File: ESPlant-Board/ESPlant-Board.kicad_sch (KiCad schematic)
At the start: 30 parts, among them J1 Conn_02x04_Counter_Clockwise, U1 ESP32-S2-MINI-1-N4, U2 BH-AAA-B5AK001, U3 Reset, U4 Boot, U5 Temp/Humid-Sensor, U6 Light sensor, U7 AMS1117-3_3, U8 MK-12C02-G025

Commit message: Update pcb for v2.0
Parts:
- removed D1: GREEN, LED_SMD:LED_0805_2012Metric, symbol Device:LED
- removed D2: ~, Diode_SMD:D_SOD-123, symbol Device:D
- removed D3: RED, LED_SMD:LED_0805_2012Metric, symbol Device:LED
- added D1: GREEN, CustomFootprints:LED0805-GREEN-RD, symbol Custom_Parts:Green-0805-LED
- added D2: SOD-123-Switching-Diode, CustomFootprints:SOD-123F_L2.7-W1.6-LS3.8-RD, symbol Custom_Parts:SOD-123-Switching-Diode
- added D3: RED, CustomFootprints:LED0805-RD_RED, symbol Custom_Parts:Red-0805-LED
- added H1, H2: MountingHole, CustomFootprints:JLCPCB_ToolingHole, symbol Mechanical:MountingHole
- added R10, R2: 5k1, Resistor_SMD:R_0402_1005Metric, symbol Device:R
- C4: now not fitted; now left out of the parts list
- U8: MPN (none) -> C778186
- USB1: now left out of the parts list
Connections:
- net +3V3: now also R10.2, R2.2
- net AD_Capacitance: now also D2.1 (K)
- net GND: now also D1.2 (K), D3.1 (-)
- net LED_GREEN: now also D1.1 (A)
- net LED_RED: now also D3.2 (+)
- net SensorCapV: now also D2.2 (A)
- net TH_SCL: now also R2.1
- net TH_SDA: now also R10.1

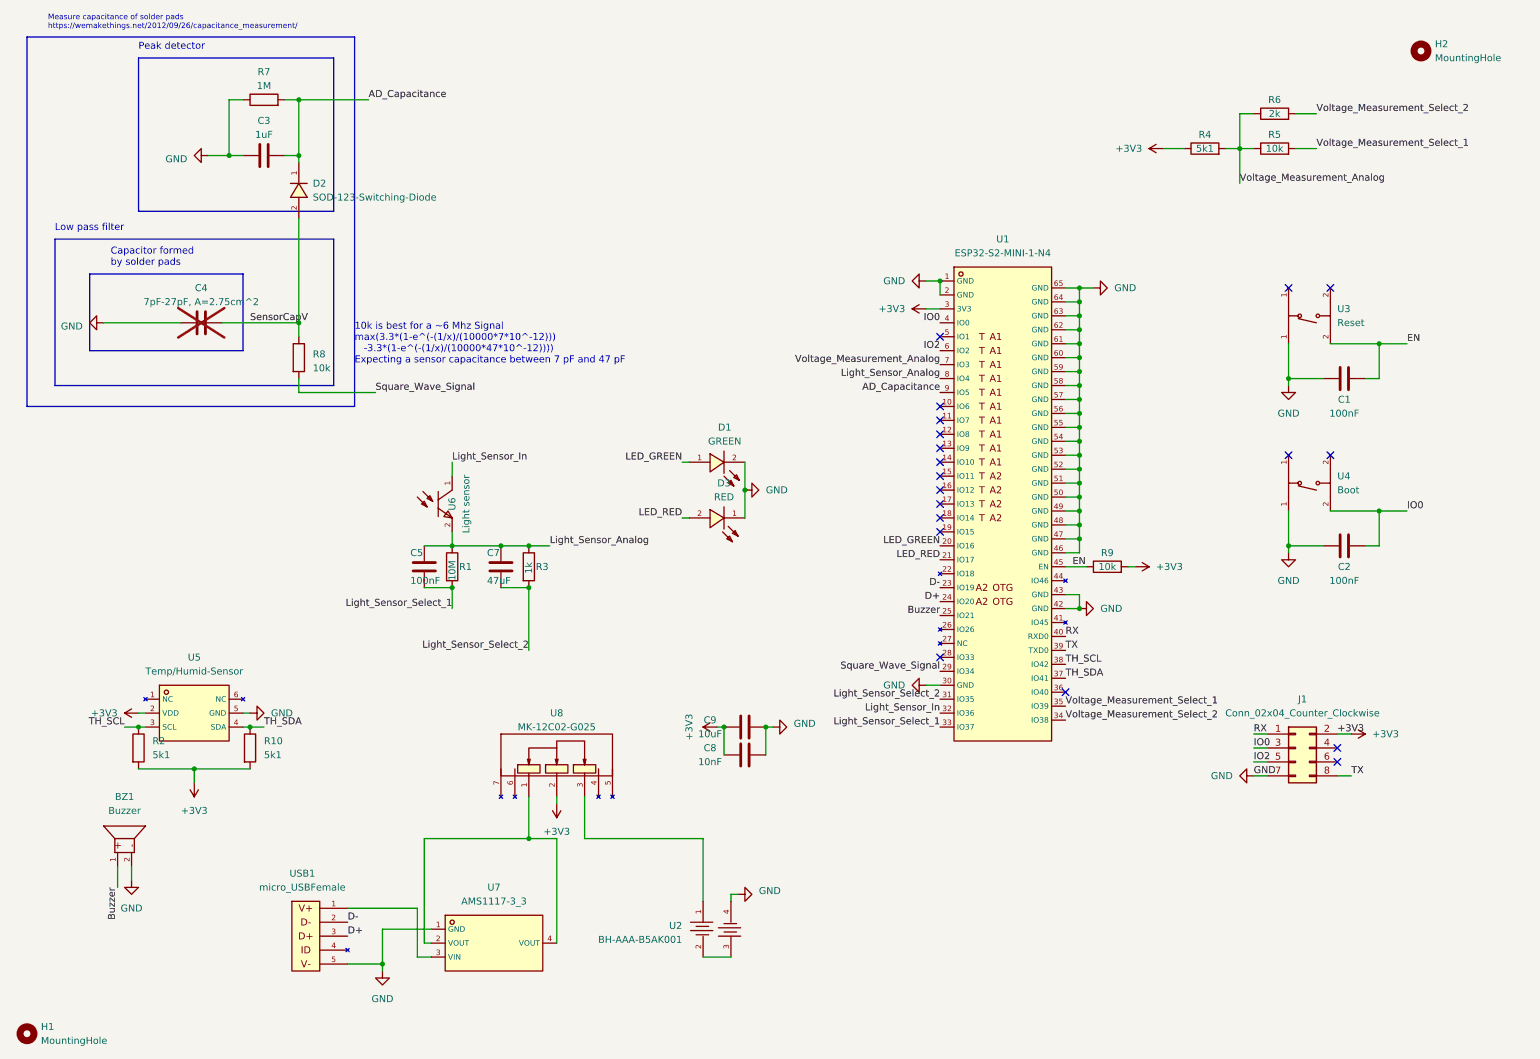
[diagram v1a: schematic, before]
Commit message: add fab layer
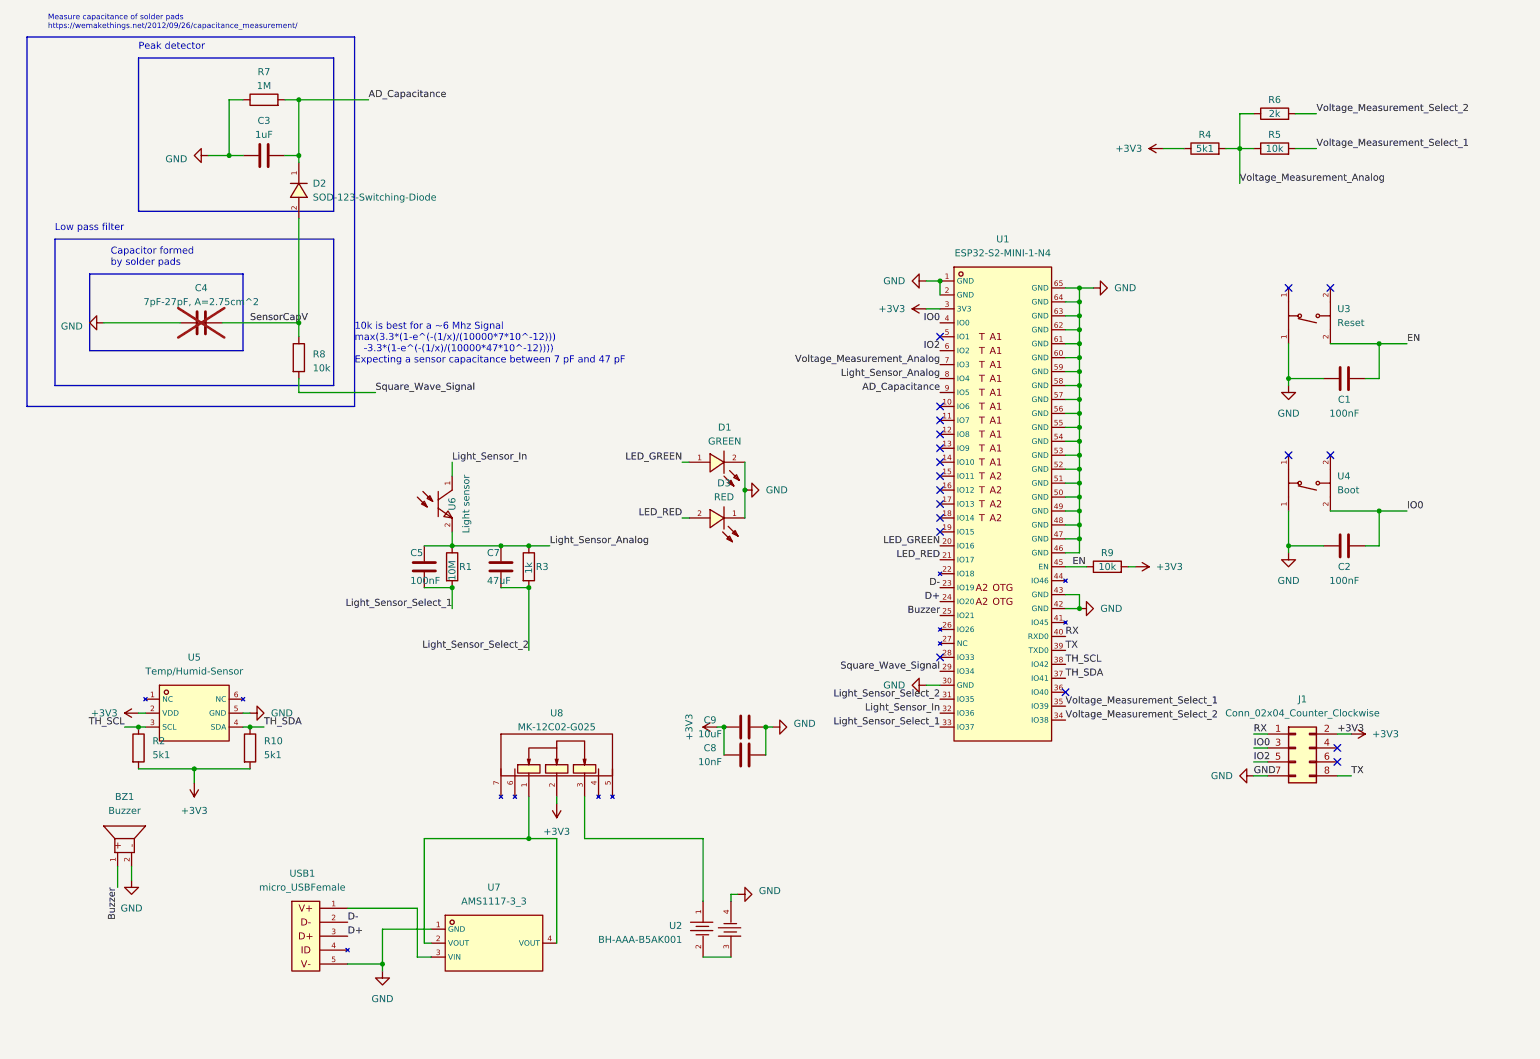
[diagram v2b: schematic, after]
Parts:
- removed H1, H2: MountingHole, CustomFootprints:JLCPCB_ToolingHole, symbol Mechanical:MountingHole
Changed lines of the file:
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@@
-    )
-  )
-  (symbol (lib_id "Mechanical:MountingHole") (at 15.24 194.31 0) (unit 1)
-    (in_bom yes) (on_board yes) (dnp no) (fields_autoplaced)
-    (property "Reference" "H1" (at 17.78 193.04 0)
-      (effects (font (size 1.27 1.27)) (justify left))
-    )
-    (property "Value" "MountingHole" (at 17.78 195.58 0)
-      (effects (font (size 1.27 1.27)) (justify left))
-    )
-    (property "Footprint" "CustomFootprints:JLCPCB_ToolingHole" (at 15.24 194.31 0)
-      (effects (font (size 1.27 1.27)) hide)
-    )
-    (property "Datasheet" "~" (at 15.24 194.31 0)
-      (effects (font (size 1.27 1.27)) hide)
-    )
-    (instances
-      (project "ESPlant-Board"
-        (path "/fa2a81f8-bf39-4c28-beef-a6fc807c4564"
-          (reference "H1") (unit 1)
-        )
-      )
     )
   )
@@
         )
       )
-    )
-  )
-  (symbol (lib_id "Mechanical:MountingHole") (at 269.24 15.24 0) (unit 1)
-    (in_bom yes) (on_board yes) (dnp no) (fields_autoplaced)
-    (property "Reference" "H2" (at 271.78 13.97 0)
-      (effects (font (size 1.27 1.27)) (justify left))
-    )
-    (property "Value" "MountingHole" (at 271.78 16.51 0)
-      (effects (font (size 1.27 1.27)) (justify left))
-    )
-    (property "Footprint" "CustomFootprints:JLCPCB_ToolingHole" (at 269.24 15.24 0)
-      (effects (font (size 1.27 1.27)) hide)
-    )
-    (property "Datasheet" "~" (at 269.24 15.24 0)
-      (effects (font (size 1.27 1.27)) hide)
-    )
-    (instances
-      (project "ESPlant-Board"
-        (path "/fa2a81f8-bf39-4c28-beef-a6fc807c4564"
-          (reference "H2") (unit 1)
-        )
-      )

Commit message: Add panel
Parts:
- J1: now left out of the parts list
- USB1: now in the parts list
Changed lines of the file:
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@@
   )
   (symbol (lib_id "Connector_Generic:Conn_02x04_Odd_Even") (at 246.38 142.24 0) (unit 1)
-    (in_bom yes) (on_board yes) (dnp no) (fields_autoplaced)
+    (in_bom no) (on_board yes) (dnp no) (fields_autoplaced)
     (property "Reference" "J1" (at 247.65 133.35 0)
       (effects (font (size 1.27 1.27)))
@@
   )
   (symbol (lib_id "Custom_Parts:micro_USBFemale") (at 64.77 176.53 0) (unit 1)
-    (in_bom no) (on_board yes) (dnp no) (fields_autoplaced)
+    (in_bom yes) (on_board yes) (dnp no) (fields_autoplaced)
     (property "Reference" "USB1" (at 65.405 165.1 0)
       (effects (font (size 1.27 1.27)))

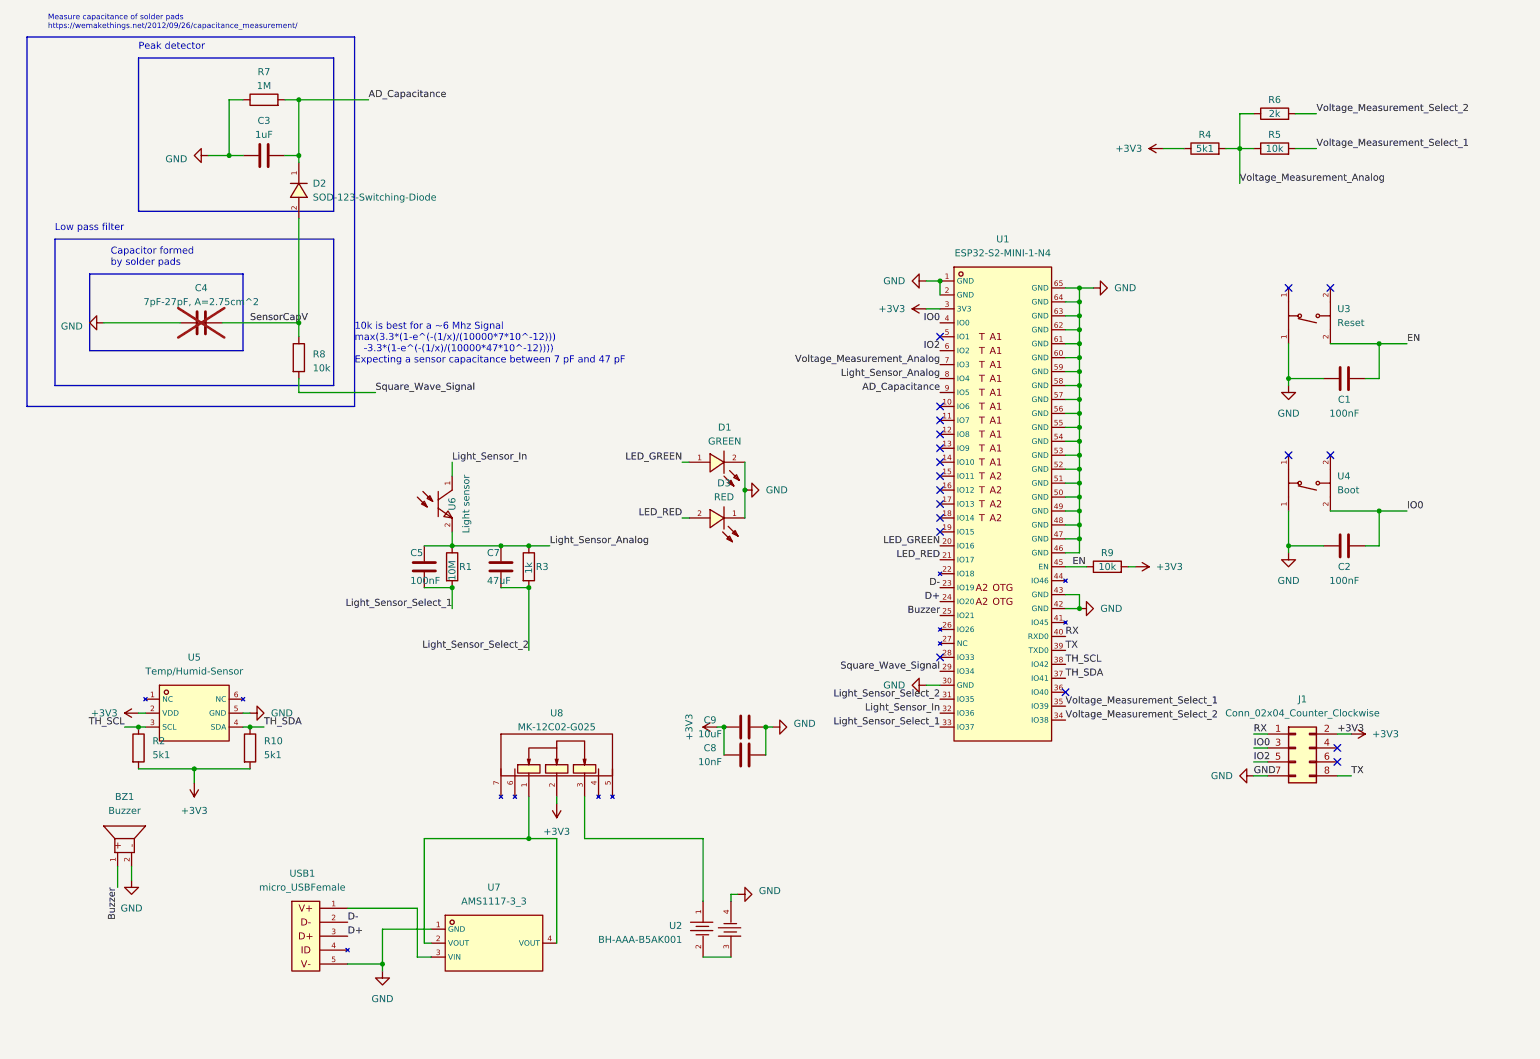
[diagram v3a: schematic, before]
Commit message: board: remove redundant parts
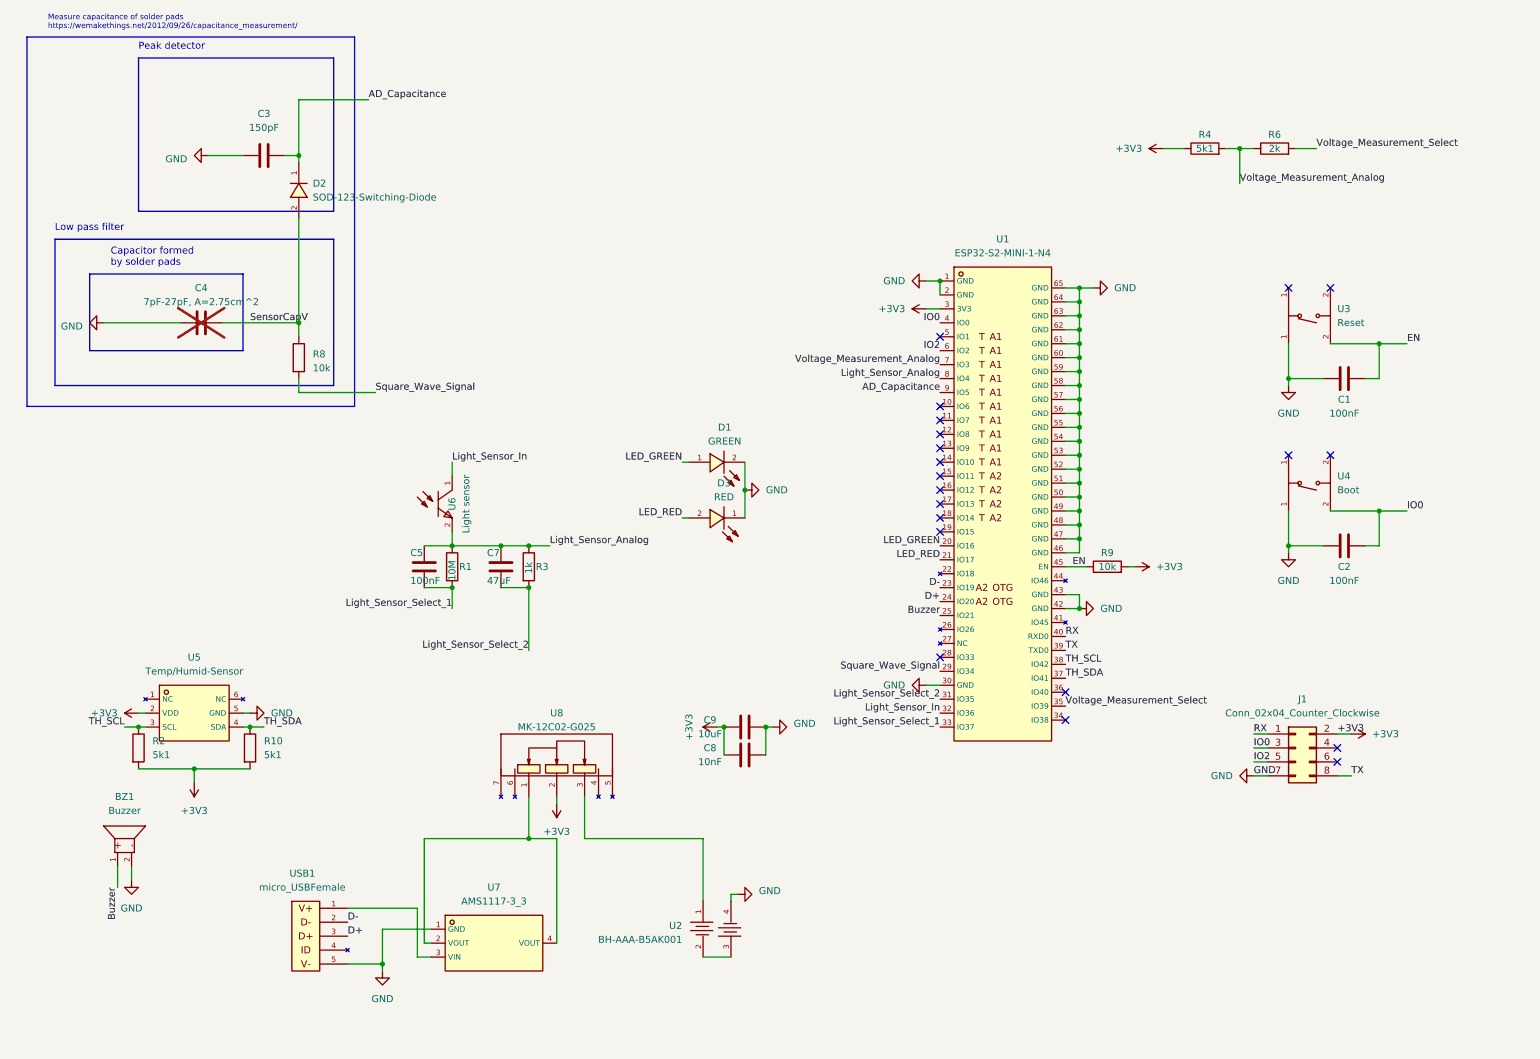
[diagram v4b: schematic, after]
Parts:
- removed R5: 10k, Resistor_SMD:R_0402_1005Metric, symbol Device:R
- removed R7: 1M, Resistor_SMD:R_0402_1005Metric, symbol Device:R
- C3: value 1uF -> 150pF; LCSC C52923 -> C1527; MPN C52923 -> C1527
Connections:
- net Voltage_Measurement_Select_1 renamed Voltage_Measurement_Select
- net Voltage_Measurement_Select: now also R6.2
- net Voltage_Measurement_Select_2: no longer names the net of U1.34 (IO38)
- net Voltage_Measurement_Select_2: no longer R6.2
- no-connect marks 19 -> 20
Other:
- note removed: "10k is best for a ~6 Mhz Signal max(3.3*(1-e^(-(1/x)/(10000*7*10^-12))) -3.3*(1-e^(-(1/x)/(10000*47*10^-12)))) Expecting a sensor capacitance between 7 pF and 47 pF"
- moved on the sheet: R6

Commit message: Board: finalize small version, Case: create file
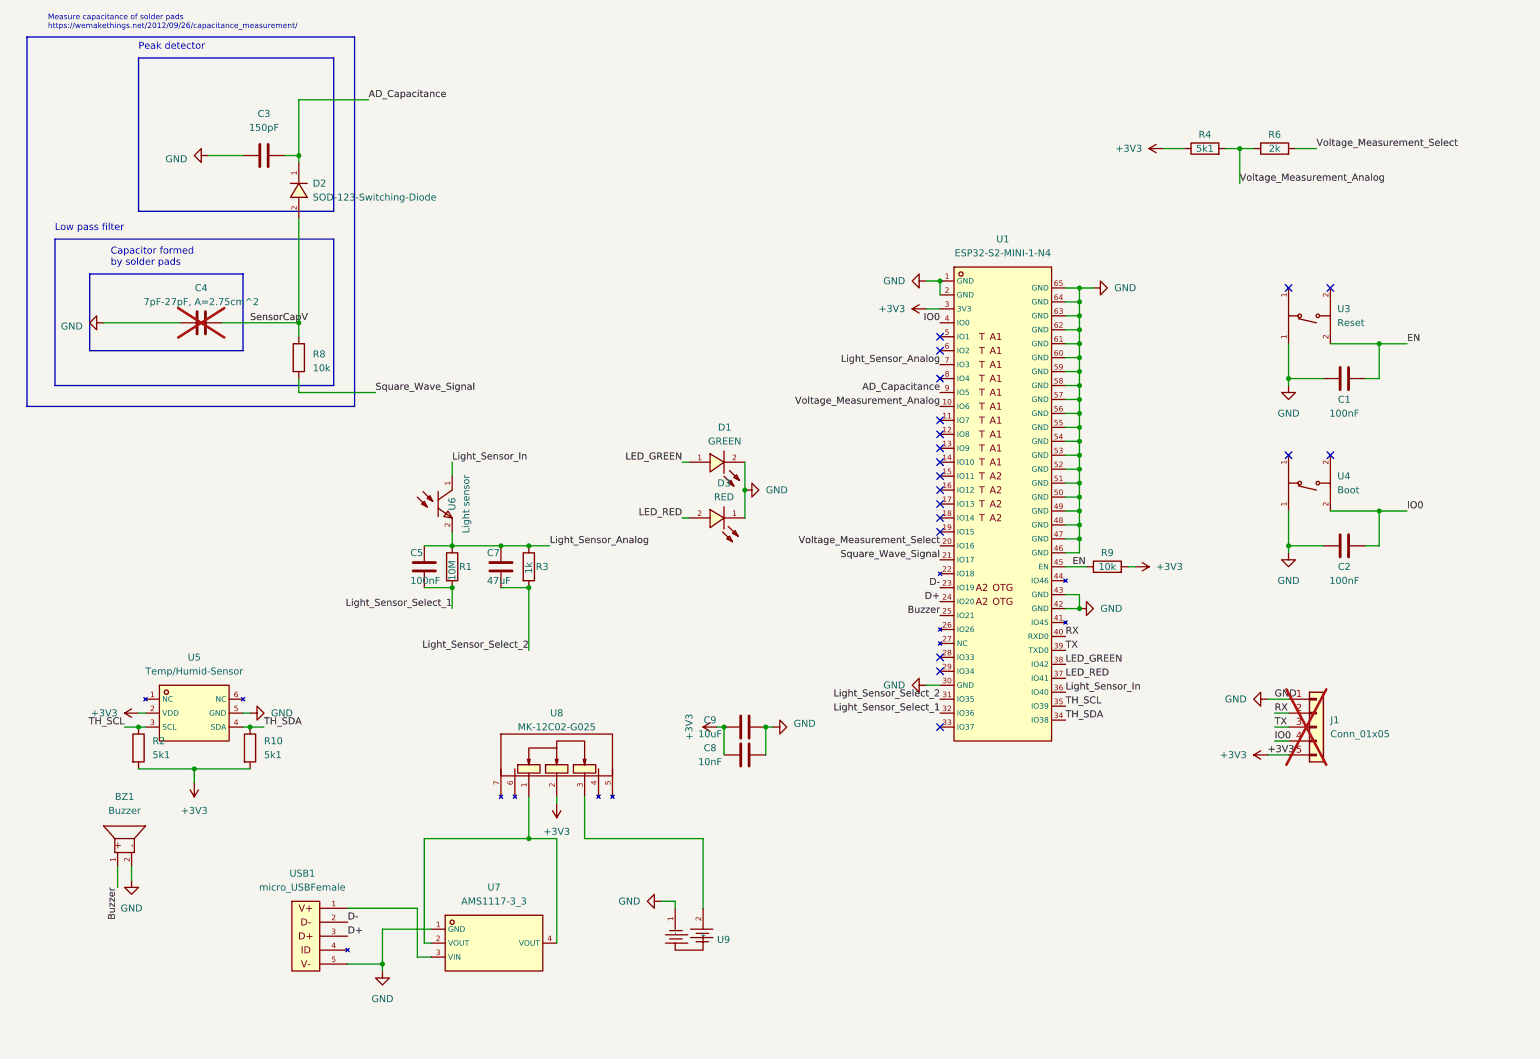
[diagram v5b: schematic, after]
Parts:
- removed J1: Conn_02x04_Counter_Clockwise, Connector_PinHeader_2.54mm:PinHeader_2x04_P2.54mm_Vertical, symbol Connector_Generic:Conn_02x04_Odd_Even
- removed U2: BH-AAA-B5AK001, CustomFootprints:BAT-SMD_BH-AAA-B5AA001, symbol Custom_Parts:BH-AAA-B5AK001
- added J1: Conn_01x05, Connector_PinHeader_2.54mm:PinHeader_1x05_P2.54mm_Vertical, symbol Connector_Generic:Conn_01x05
- added U9: ~, CustomFootprints:AAA Battery-spring, symbol Custom_Parts:AAA_Battery-Spring
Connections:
- net +3V3: now also J1.5 (Pin_5)
- net GND: now also J1.1 (Pin_1), U9.1 (-)
- net IO0: now also J1.4 (Pin_4)
- net LED_GREEN: now also U1.38 (IO42); no longer U1.20 (IO16)
- net LED_RED: now also U1.37 (IO41); no longer U1.21 (IO17)
- net Light_Sensor_Analog: now also U1.7 (IO3); no longer U1.8 (IO4)
- net Light_Sensor_In: now also U1.36 (IO40); no longer U1.32 (IO36)
- net Light_Sensor_Select_1: now also U1.32 (IO36); no longer U1.33 (IO37)
- net RX: now also J1.2 (Pin_2)
- net Square_Wave_Signal: now also U1.21 (IO17); no longer U1.29 (IO34)
- net TH_SCL: now also U1.35 (IO39); no longer U1.38 (IO42)
- net TH_SDA: now also U1.34 (IO38); no longer U1.37 (IO41)
- net TX: now also J1.3 (Pin_3)
- net Voltage_Measurement_Analog: now also U1.10 (IO6); no longer U1.7 (IO3)
- net Voltage_Measurement_Select: now also U1.20 (IO16); no longer U1.35 (IO39)
- net at U8.3: now also U9.2 (+)
- net IO2: no longer names the net of U1.6 (IO2)
- no-connect marks 20 -> 19
